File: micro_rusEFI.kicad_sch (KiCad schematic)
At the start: 57 parts, among them J12 Conn_01x01, J13 Conn_01x01, J3 Conn_01x01, J4 Conn_02x05_Counter_Clockwise, J5 Conn_01x01, U3 molex_48pin_MRE, U7 XC6206 3.3V

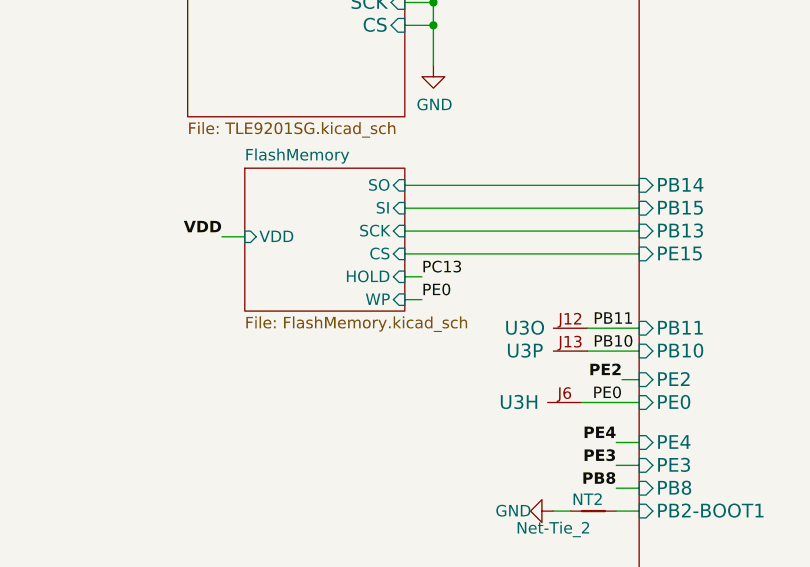
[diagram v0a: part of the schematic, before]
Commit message: Small pcb fix
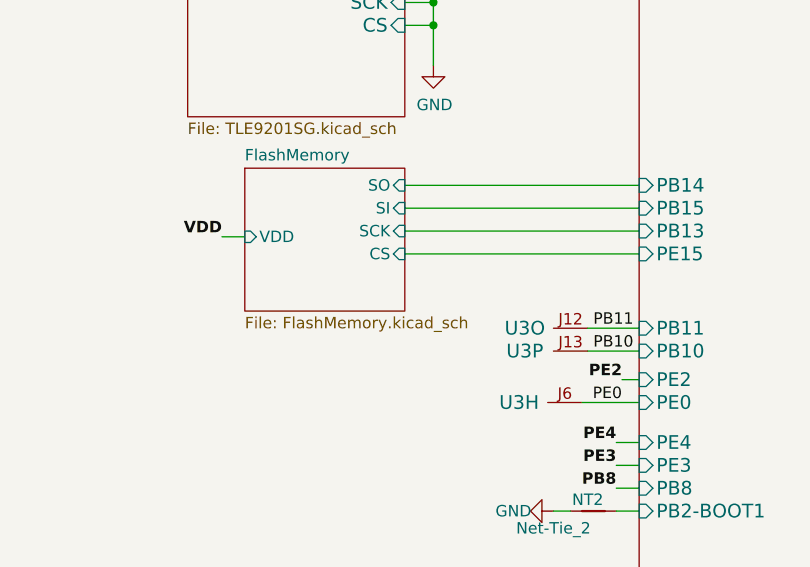
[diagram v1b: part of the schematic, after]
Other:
- sheet FlashMemory ports: added none; removed HOLD, WP
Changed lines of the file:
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@@
     (stroke (width 0) (type default) (color 0 0 0 0))
   )
-  (wire (pts (xy 144.145 198.12) (xy 146.05 198.12))
-    (stroke (width 0) (type default) (color 0 0 0 0))
-  )
   (wire (pts (xy 209.55 40.005) (xy 209.55 41.91))
     (stroke (width 0) (type default) (color 0 0 0 0))
@@
     (stroke (width 0) (type default) (color 0 0 0 0))
   )
-  (wire (pts (xy 144.145 200.66) (xy 146.05 200.66))
-    (stroke (width 0) (type default) (color 0 0 0 0))
-  )
   (polyline (pts (xy 307.975 219.075) (xy 307.975 225.425))
     (stroke (width 0) (type default) (color 0 0 0 0))
@@
     (effects (font (size 1.524 1.524) (thickness 0.3048) bold) (justify left bottom))
   )
-  (label "PE0" (at 146.05 200.66 0)
-    (effects (font (size 1.27 1.27)) (justify left bottom))
-  )
   (label "CS_TLE" (at 228.6 130.175 180)
     (effects (font (size 1.524 1.524) (thickness 0.3048) bold) (justify right bottom))
@@
     (effects (font (size 1.524 1.524) (thickness 0.3048) bold) (justify right bottom))
   )
-  (label "PC13" (at 146.05 198.12 0)
-    (effects (font (size 1.27 1.27)) (justify left bottom))
-  )
   (label "AV6" (at 363.855 223.52 0)
     (effects (font (size 1.27 1.27)) (justify left bottom))
@@
       (effects (font (size 1.27 1.27)) (justify left))
     )
-    (pin "HOLD" input (at 144.145 198.12 0)
-      (effects (font (size 1.27 1.27)) (justify right))
-    )
-    (pin "WP" input (at 144.145 200.66 0)
-      (effects (font (size 1.27 1.27)) (justify right))
-    )
   )

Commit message: KiCAD6 version
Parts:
- added D44: 1N4148WS, Diode_SMD:D_SOD-323, symbol Diode:1N4148WS
- added JP3: Voltage selector 5V 3V3, Jumper:SolderJumper-3_P1.3mm_Bridged12_RoundedPad1.0x1.5mm, symbol Jumper:SolderJumper_3_Open
- added unit 19 of U3
- added unit 17 of U3
- added unit 18 of U3
- U3: footprint rusefi_lib:Molex_48_MRE -> rusefi_lib:Molex_48_MRE_R055; Manufacturer MOLEX -> (none); Part # 500762-0481 -> (none); VEND DIGI -> (none); VEND# WM4430-ND -> (none)
- U3: footprint rusefi_lib:Molex_48_MRE -> rusefi_lib:Molex_48_MRE_R055
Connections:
- net 5V: now also JP3.3 (B)
- net CANH: now also U3.J22, U3.J49
- net CANL: now also U3.J23, U3.J50
- net GND: now also U3.J20
- net VDD: now also D44.2 (A)
- new net: JP3.2 (C), U3.J21
- new net: D44.1 (K), JP3.1 (A)
- no-connect marks 20 -> 22

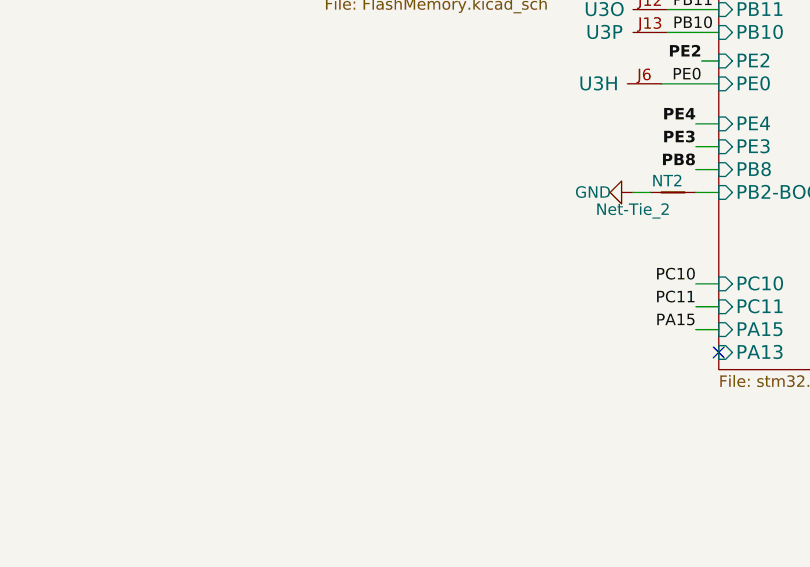
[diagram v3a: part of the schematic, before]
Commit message: Dual footprint for SDCard - SPI2 & SPI3
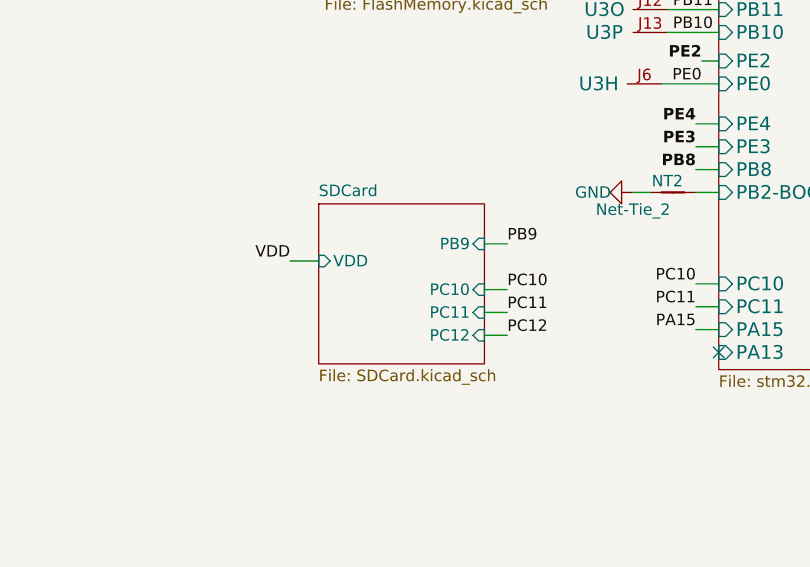
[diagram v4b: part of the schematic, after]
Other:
- added sheet SDCard (SDCard.kicad_sch)
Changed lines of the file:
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@@
     (stroke (width 0) (type default) (color 0 0 0 0))
   )
+  (wire (pts (xy 125.73 231.775) (xy 122.555 231.775))
+    (stroke (width 0) (type default) (color 0 0 0 0))
+  )
   (wire (pts (xy 170.18 234.315) (xy 167.64 234.315))
     (stroke (width 0) (type default) (color 0 0 0 0))
@@
     (stroke (width 0) (type default) (color 0 0 0 0))
   )
+  (wire (pts (xy 144.145 237.49) (xy 146.685 237.49))
+    (stroke (width 0) (type default) (color 0 0 0 0))
+  )
   (wire (pts (xy 340.36 59.69) (xy 341.63 59.69))
     (stroke (width 0) (type default) (color 0 0 0 0))
@@
     (stroke (width 0) (type default) (color 0 0 0 0))
   )
+  (wire (pts (xy 144.145 240.03) (xy 146.685 240.03))
+    (stroke (width 0) (type default) (color 0 0 0 0))
+  )
   (wire (pts (xy 228.6 109.855) (xy 201.93 109.855))
     (stroke (width 0) (type default) (color 0 0 0 0))
@@
     (stroke (width 0) (type default) (color 0 0 0 0))
   )
+  (wire (pts (xy 144.145 234.95) (xy 146.685 234.95))
+    (stroke (width 0) (type default) (color 0 0 0 0))
+  )
   (wire (pts (xy 86.995 104.775) (xy 102.87 104.775))
     (stroke (width 0) (type default) (color 0 0 0 0))
@@
     (stroke (width 0) (type default) (color 0 0 0 0))
   )
+  (wire (pts (xy 144.145 229.87) (xy 146.685 229.87))
+    (stroke (width 0) (type default) (color 0 0 0 0))
+  )
   (wire (pts (xy 273.05 114.935) (xy 325.755 114.935))
     (stroke (width 0) (type default) (color 0 0 0 0))
@@
     (effects (font (size 1.524 1.524) (thickness 0.3048) bold) (justify right bottom))
   )
+  (label "VDD" (at 122.555 231.775 180)
+    (effects (font (size 1.27 1.27)) (justify right bottom))
+  )
   (label "AT3" (at 184.15 41.91 270)
     (effects (font (size 1.524 1.524) (thickness 0.3048) bold) (justify right bottom))
@@
     (effects (font (size 1.524 1.524) (thickness 0.3048) bold) (justify left bottom))
   )
+  (label "PC11" (at 146.685 237.49 0)
+    (effects (font (size 1.27 1.27)) (justify left bottom))
+  )
   (label "INJECTOR-2" (at 296.545 102.235 0)
     (effects (font (size 1.524 1.524) (thickness 0.3048) bold) (justify left bottom))
@@
     (effects (font (size 1.524 1.524) (thickness 0.3048) bold) (justify right bottom))
   )
+  (label "PB9" (at 146.685 229.87 0)
+    (effects (font (size 1.27 1.27)) (justify left bottom))
+  )
   (label "VDD" (at 118.11 160.655 180)
     (effects (font (size 1.524 1.524) (thickness 0.3048) bold) (justify right bottom))
@@
     (effects (font (size 1.27 1.27)) (justify right bottom))
   )
+  (label "PC12" (at 146.685 240.03 0)
+    (effects (font (size 1.27 1.27)) (justify left bottom))
+  )
   (label "TLE_DFB13" (at 277.495 196.215 0)
     (effects (font (size 1.27 1.27)) (justify left bottom))
@@
     (effects (font (size 1.27 1.27)) (justify left bottom))
   )
+  (label "PC10" (at 146.685 234.95 0)
+    (effects (font (size 1.27 1.27)) (justify left bottom))
+  )
   (label "AV1" (at 191.77 41.91 270)
     (effects (font (size 1.524 1.524) (thickness 0.3048) bold) (justify right bottom))
@@
     )
   )
+  (sheet (at 125.73 225.425) (size 18.415 17.78) (fields_autoplaced)
+    (stroke (width 0) (type solid) (color 0 0 0 0))
+    (fill (color 0 0 0 0.0000))
+    (property "Sheet name" "SDCard" (id 0) (at 125.73 224.7134 0)
+      (effects (font (size 1.27 1.27)) (justify left bottom))
+    )
+    (property "Sheet file" "SDCard.kicad_sch" (id 1) (at 125.73 243.7896 0)
+      (effects (font (size 1.27 1.27)) (justify left top))
+    )
+    (pin "VDD" input (at 125.73 231.775 180)
+      (effects (font (size 1.27 1.27)) (justify left))
+    )
+    (pin "PB9" input (at 144.145 229.87 0)
+      (effects (font (size 1.27 1.27)) (justify right))
+    )
+    (pin "PC10" input (at 144.145 234.95 0)
+      (effects (font (size 1.27 1.27)) (justify right))
+    )
+    (pin "PC11" input (at 144.145 237.49 0)
+      (effects (font (size 1.27 1.27)) (justify right))
+    )
+    (pin "PC12" input (at 144.145 240.03 0)
+      (effects (font (size 1.27 1.27)) (justify right))
+    )
+  )
   (sheet_instances
     (path "/" (page "1"))
@@
     (path "/00000000-0000-0000-0000-00005c5d7fa6" (page "8"))
     (path "/00000000-0000-0000-0000-00005cbdf691" (page "9"))
+    (path "/d7393ec0-523a-428c-a869-c2bcf3379fa8" (page "10"))
   )
   (symbol_instances
@@
       (reference "#PWR0129") (unit 1) (value "GND") (footprint "")
     )
+    (path "/d7393ec0-523a-428c-a869-c2bcf3379fa8/00000000-0000-0000-0000-00005d2f3d06"
+      (reference "#PWR0130") (unit 1) (value "~") (footprint "")
+    )
     (path "/00000000-0000-0000-0000-00005d0250fb/00000000-0000-0000-0000-00005c5e3a23"
       (reference "#PWR0131") (unit 1) (value "GND") (footprint "")
@@
       (reference "#PWR0133") (unit 1) (value "GND") (footprint "")
     )
+    (path "/d7393ec0-523a-428c-a869-c2bcf3379fa8/00000000-0000-0000-0000-0000618f24cd"
+      (reference "#PWR0134") (unit 1) (value "~") (footprint "")
+    )
+    (path "/d7393ec0-523a-428c-a869-c2bcf3379fa8/00000000-0000-0000-0000-0000618f24ce"
+      (reference "#PWR0135") (unit 1) (value "~") (footprint "")
+    )
     (path "/00000000-0000-0000-0000-00005ce2282d/00000000-0000-0000-0000-00005d0dddd4"
       (reference "#PWR0136") (unit 1) (value "GND") (footprint "")
@@
       (reference "C42") (unit 1) (value "100nF") (footprint "Capacitor_SMD:C_0603_1608Metric")
     )
+    (path "/d7393ec0-523a-428c-a869-c2bcf3379fa8/00000000-0000-0000-0000-0000618f24c8"
+      (reference "C42") (unit 1) (value "~") (footprint "")
+    )
     (path "/00000000-0000-0000-0000-00005c5d7fa6/00000000-0000-0000-0000-00005d8748d4"
       (reference "C43") (unit 1) (value "22uF 25V") (footprint "Capacitor_SMD:C_0805_2012Metric")
@@
       (reference "J13") (unit 1) (value "Conn_01x01") (footprint "Connector_Pin:Pin_D0.7mm_L6.5mm_W1.8mm_FlatFork")
     )
+    (path "/d7393ec0-523a-428c-a869-c2bcf3379fa8/00000000-0000-0000-0000-00005f3076e2"
+      (reference "J14") (unit 1) (value "~") (footprint "")
+    )
     (path "/00000000-0000-0000-0000-00005c5d7fa6/00000000-0000-0000-0000-00005ea3f4b2"

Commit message: R0.6.1rc KICAD6
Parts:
- R86: footprint Resistor_SMD:R_0805_2012Metric -> Resistor_SMD:R_0603_1608Metric
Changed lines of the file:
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@@
     )
     (property "Value" "0R" (id 1) (at 311.785 223.52 90))
-    (property "Footprint" "Resistor_SMD:R_0805_2012Metric" (id 2) (at 311.785 221.742 90)
+    (property "Footprint" "Resistor_SMD:R_0603_1608Metric" (id 2) (at 311.785 221.742 90)
       (effects (font (size 1.27 1.27)) hide)
     )
@@
       (reference "#PWR0129") (unit 1) (value "GND") (footprint "")
     )
-    (path "/d7393ec0-523a-428c-a869-c2bcf3379fa8/00000000-0000-0000-0000-00005d2f3d06"
-      (reference "#PWR0130") (unit 1) (value "~") (footprint "")
-    )
     (path "/00000000-0000-0000-0000-00005d0250fb/00000000-0000-0000-0000-00005c5e3a23"
       (reference "#PWR0131") (unit 1) (value "GND") (footprint "")
@@
       (reference "C42") (unit 1) (value "100nF") (footprint "Capacitor_SMD:C_0603_1608Metric")
     )
-    (path "/d7393ec0-523a-428c-a869-c2bcf3379fa8/00000000-0000-0000-0000-0000618f24c8"
-      (reference "C42") (unit 1) (value "~") (footprint "")
-    )
     (path "/00000000-0000-0000-0000-00005c5d7fa6/00000000-0000-0000-0000-00005d8748d4"
       (reference "C43") (unit 1) (value "22uF 25V") (footprint "Capacitor_SMD:C_0805_2012Metric")
@@
     )
     (path "/d7393ec0-523a-428c-a869-c2bcf3379fa8/00000000-0000-0000-0000-00005f3076e2"
-      (reference "J14") (unit 1) (value "~") (footprint "")
+      (reference "J14") (unit 1) (value "~") (footprint "Connector_Card:microSD_HC_Wuerth_693072010801")
     )
     (path "/00000000-0000-0000-0000-00005c5d7fa6/00000000-0000-0000-0000-00005ea3f4b2"
@@
     )
     (path "/00000000-0000-0000-0000-00005c5d7fa6/00000000-0000-0000-0000-00005cc90402"
-      (reference "R3") (unit 1) (value "10K") (footprint "Resistor_SMD:R_0805_2012Metric")
+      (reference "R3") (unit 1) (value "10K") (footprint "Resistor_SMD:R_0603_1608Metric")
     )
     (path "/00000000-0000-0000-0000-00005c5d7fa6/00000000-0000-0000-0000-00005cc7ae36"
@@
     )
     (path "/00000000-0000-0000-0000-00005eeecfe7"
-      (reference "R86") (unit 1) (value "0R") (footprint "Resistor_SMD:R_0805_2012Metric")
+      (reference "R86") (unit 1) (value "0R") (footprint "Resistor_SMD:R_0603_1608Metric")
     )
     (path "/00000000-0000-0000-0000-00005cbdf691/00000000-0000-0000-0000-00005d157560"
